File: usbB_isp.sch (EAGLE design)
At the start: 12 parts, among them IC1 788TV, IC2 TINY13-20PU, X1 PN61729-S

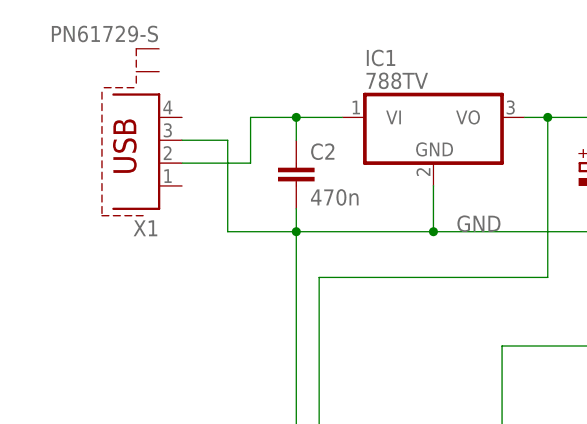
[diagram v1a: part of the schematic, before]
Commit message: fixing mass pin
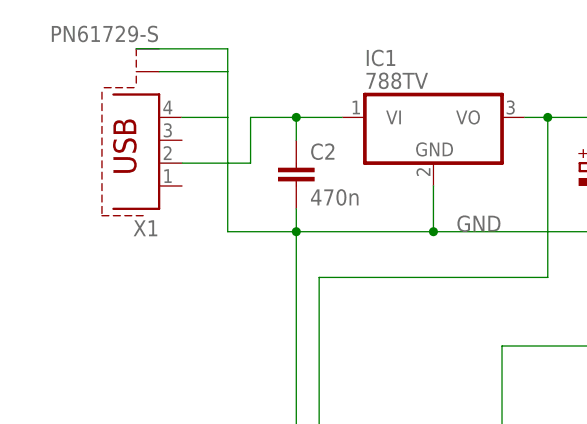
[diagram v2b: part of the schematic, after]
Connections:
- net GND: now also X1.4, X1.S1; no longer X1.3
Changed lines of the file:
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@@
 <wire x1="152.4" y1="20.32" x2="40.64" y2="20.32" width="0.1524" layer="91"/>
 <junction x="40.64" y="30.48"/>
-<pinref part="X1" gate="G$1" pin="3"/>
-<wire x1="-5.08" y1="68.58" x2="0" y2="68.58" width="0.1524" layer="91"/>
-<wire x1="0" y1="68.58" x2="0" y2="58.42" width="0.1524" layer="91"/>
 <wire x1="0" y1="58.42" x2="7.62" y2="58.42" width="0.1524" layer="91"/>
 <wire x1="7.62" y1="58.42" x2="7.62" y2="60.96" width="0.1524" layer="91"/>
@@
 <junction x="152.4" y="58.42"/>
 <wire x1="152.4" y1="48.26" x2="152.4" y2="58.42" width="0.1524" layer="91"/>
+<wire x1="0" y1="58.42" x2="0" y2="71.12" width="0.1524" layer="91"/>
+<pinref part="X1" gate="G$1" pin="4"/>
+<wire x1="0" y1="71.12" x2="-5.08" y2="71.12" width="0.1524" layer="91"/>
+<wire x1="0" y1="71.12" x2="0" y2="76.2" width="0.1524" layer="91"/>
+<pinref part="X1" gate="G$1" pin="S1"/>
+<wire x1="-7.62" y1="76.2" x2="0" y2="76.2" width="0.1524" layer="91"/>
+<wire x1="0" y1="76.2" x2="0" y2="78.74" width="0.1524" layer="91"/>
+<wire x1="0" y1="78.74" x2="-10.16" y2="78.74" width="0.1524" layer="91"/>
 </segment>
 </net>
